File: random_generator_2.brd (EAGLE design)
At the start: 19.1 x 19.1 mm, 17 parts, among them IC1 OPA2340U

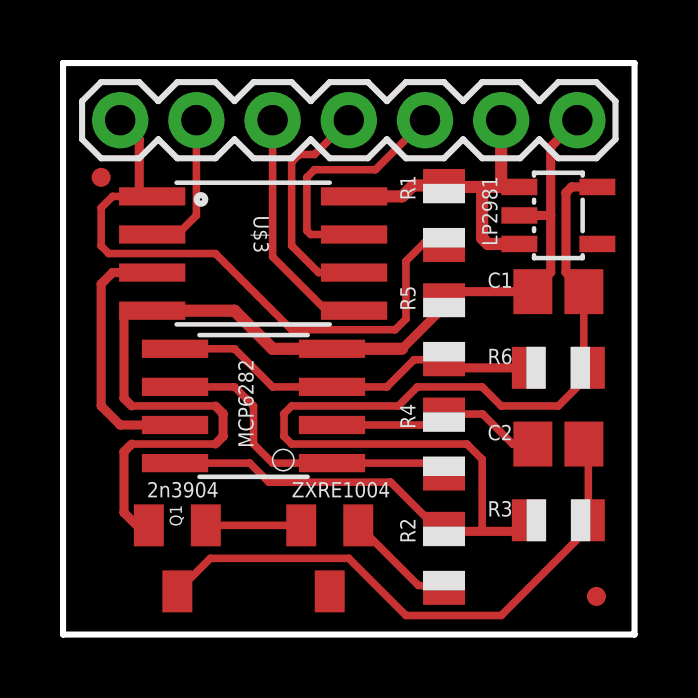
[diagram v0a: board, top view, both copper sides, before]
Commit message: MANY BUGS! NOW, HANDLE IT!
A whole nightmarish mess of bugs fixed: Dr Nyquist prescribed some
faster sampling, (just in case). I also tied op amp to VCCIO instead of
3V (for voltage swings guaranteed to trigger logic high), SPI/USI code
now works too. WIll upload an Arduino test program soon…
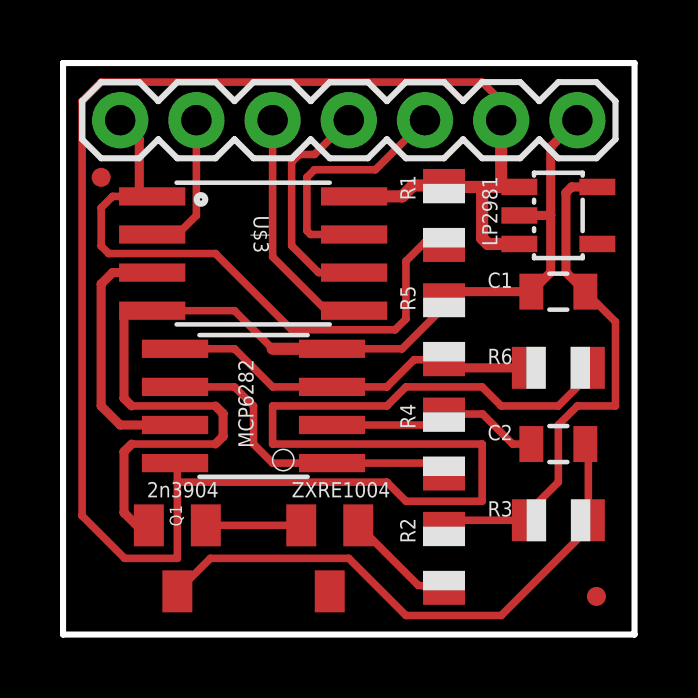
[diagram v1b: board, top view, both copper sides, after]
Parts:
- C1: device adafruit:C0805 -> SparkFun:0805
- C2: value .1uF -> 1uF; device adafruit:C0805 -> SparkFun:0805
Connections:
- net V+: no longer IC1.8, R6.2
- net VCCIO: now also IC1.8, R6.2
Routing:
- net VCCIO: track 11.5 -> 79.8 mm
- net V+: track 43.6 -> 17.6 mm
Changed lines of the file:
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@@
 <setting verticaltext="up"/>
 </settings>
-<grid distance="0.05" unitdist="inch" unit="inch" style="lines" multiple="1" display="yes" altdistance="0.01" altunitdist="inch" altunit="inch"/>
+<grid distance="0.05" unitdist="inch" unit="inch" style="lines" multiple="1" display="yes" altdistance="0.025" altunitdist="inch" altunit="inch"/>
 <layers>
 <layer number="1" name="Top" color="4" fill="1" visible="yes" active="yes"/>
@@
 <attribute name="VALUE" x="14.986" y="8.89" size="0.508" layer="27" font="vector" rot="R180"/>
 </element>
-<element name="C2" library="adafruit" package="C0805" value=".1uF" x="16.51" y="6.35" smashed="yes" rot="R180">
+<element name="C2" library="SparkFun" package="0805" value="1uF" x="16.51" y="6.35" smashed="yes" rot="R180">
 <attribute name="NAME" x="14.986" y="6.985" size="0.508" layer="25" font="vector" rot="R180"/>
 <attribute name="VALUE" x="14.986" y="6.35" size="0.508" layer="27" font="vector" rot="R180"/>
 </element>
 <element name="U$2" library="hjohnson_library" package="SOT23-5L" value="TC1014" x="16.51" y="13.97" smashed="yes" rot="R270"/>
-<element name="C1" library="adafruit" package="C0805" value="1uF" x="16.51" y="11.43" smashed="yes" rot="R180">
+<element name="C1" library="SparkFun" package="0805" value="1uF" x="16.51" y="11.43" smashed="yes" rot="R180">
 <attribute name="NAME" x="14.986" y="12.065" size="0.508" layer="25" font="vector" rot="R180"/>
 <attribute name="VALUE" x="14.986" y="11.43" size="0.508" layer="27" font="vector" rot="R180"/>
@@
 <wire x1="5.08" y1="7.62" x2="2.286" y2="7.62" width="0.254" layer="1"/>
 <wire x1="8.9662" y1="9.525" x2="6.985" y2="9.525" width="0.4064" layer="1"/>
-<wire x1="6.985" y1="9.525" x2="5.715" y2="10.795" width="0.4064" layer="1"/>
-<wire x1="5.715" y1="10.795" x2="2.9718" y2="10.795" width="0.4064" layer="1"/>
-<wire x1="8.9662" y1="9.525" x2="11.303" y2="9.525" width="0.4064" layer="1"/>
+<wire x1="6.985" y1="9.525" x2="5.715" y2="10.795" width="0.254" layer="1"/>
+<wire x1="5.715" y1="10.795" x2="2.9718" y2="10.795" width="0.254" layer="1"/>
+<wire x1="8.9662" y1="9.525" x2="11.303" y2="9.525" width="0.254" layer="1"/>
 <wire x1="12.7" y1="11.16" x2="12.7" y2="10.922" width="0.254" layer="1"/>
-<wire x1="12.7" y1="10.922" x2="11.303" y2="9.525" width="0.3048" layer="1"/>
+<wire x1="12.7" y1="10.922" x2="11.303" y2="9.525" width="0.254" layer="1"/>
 <contactref element="JP1" pad="7"/>
-<wire x1="16.256" y1="12.076" x2="15.66" y2="11.43" width="0.3048" layer="1"/>
+<wire x1="16.256" y1="12.076" x2="15.61" y2="11.43" width="0.3048" layer="1"/>
 <wire x1="17.145" y1="17.145" x2="16.256" y2="16.256" width="0.3048" layer="1"/>
 <wire x1="16.256" y1="16.256" x2="16.256" y2="13.97" width="0.3048" layer="1"/>
 <wire x1="16.256" y1="13.97" x2="16.256" y2="12.076" width="0.3048" layer="1"/>
 <wire x1="15.21" y1="13.97" x2="16.256" y2="13.97" width="0.3048" layer="1"/>
-<wire x1="15.66" y1="11.43" x2="12.97" y2="11.43" width="0.3048" layer="1"/>
+<wire x1="15.61" y1="11.43" x2="12.97" y2="11.43" width="0.3048" layer="1"/>
 <wire x1="12.97" y1="11.43" x2="12.7" y2="11.16" width="0.3048" layer="1"/>
 </signal>
@@
 <contactref element="R2" pad="2"/>
 <contactref element="R3" pad="2"/>
-<contactref element="R6" pad="2"/>
 <contactref element="U$2" pad="5"/>
 <contactref element="C1" pad="1"/>
-<contactref element="IC1" pad="8"/>
-<contactref element="IC1" pad="8"/>
-<wire x1="15.51" y1="3.81" x2="15.748" y2="3.81" width="0.254" layer="1"/>
-<wire x1="6.858" y1="5.08" x2="10.922" y2="5.08" width="0.254" layer="1"/>
-<wire x1="10.922" y1="5.08" x2="12.7" y2="3.302" width="0.254" layer="1"/>
-<wire x1="12.7" y1="3.54" x2="12.7" y2="3.302" width="0.254" layer="1"/>
-<wire x1="15.378" y1="3.44" x2="15.748" y2="3.81" width="0.2032" layer="1"/>
 <wire x1="17.81" y1="14.92" x2="16.952" y2="14.92" width="0.3048" layer="1"/>
 <wire x1="16.764" y1="14.732" x2="16.764" y2="12.076" width="0.3048" layer="1"/>
-<wire x1="16.764" y1="12.076" x2="17.36" y2="11.43" width="0.3048" layer="1"/>
+<wire x1="16.764" y1="12.076" x2="17.41" y2="11.43" width="0.3048" layer="1"/>
 <wire x1="16.952" y1="14.92" x2="16.764" y2="14.732" width="0.3048" layer="1"/>
-<wire x1="15.378" y1="3.44" x2="12.8" y2="3.44" width="0.3048" layer="1"/>
-<wire x1="12.8" y1="3.44" x2="12.7" y2="3.54" width="0.254" layer="1"/>
-<wire x1="17.51" y1="8.89" x2="17.36" y2="8.89" width="0.254" layer="1"/>
-<wire x1="17.36" y1="8.89" x2="17.36" y2="11.43" width="0.254" layer="1"/>
-<wire x1="17.36" y1="8.89" x2="17.36" y2="8.47" width="0.254" layer="1"/>
-<wire x1="17.36" y1="8.47" x2="16.51" y2="7.62" width="0.254" layer="1"/>
-<wire x1="16.51" y1="7.62" x2="14.605" y2="7.62" width="0.254" layer="1"/>
-<wire x1="14.605" y1="7.62" x2="13.97" y2="8.255" width="0.254" layer="1"/>
-<wire x1="13.462" y1="6.35" x2="13.97" y2="5.842" width="0.254" layer="1"/>
-<wire x1="13.97" y1="5.842" x2="13.97" y2="3.556" width="0.254" layer="1"/>
-<wire x1="12.8" y1="3.44" x2="13.854" y2="3.44" width="0.254" layer="1"/>
-<wire x1="13.854" y1="3.44" x2="13.97" y2="3.556" width="0.254" layer="1"/>
-<wire x1="13.97" y1="8.255" x2="11.811" y2="8.255" width="0.254" layer="1"/>
-<wire x1="11.811" y1="8.255" x2="11.176" y2="7.62" width="0.254" layer="1"/>
-<wire x1="13.462" y1="6.35" x2="7.62" y2="6.35" width="0.254" layer="1"/>
-<wire x1="7.62" y1="6.35" x2="7.366" y2="6.604" width="0.254" layer="1"/>
-<wire x1="7.366" y1="6.604" x2="7.366" y2="7.366" width="0.254" layer="1"/>
-<wire x1="7.62" y1="7.62" x2="11.176" y2="7.62" width="0.254" layer="1"/>
-<wire x1="3.7338" y1="5.715" x2="6.223" y2="5.715" width="0.254" layer="1"/>
-<wire x1="6.223" y1="5.715" x2="6.858" y2="5.08" width="0.254" layer="1"/>
-<wire x1="7.366" y1="7.366" x2="7.62" y2="7.62" width="0.254" layer="1"/>
+<wire x1="15.51" y1="3.81" x2="12.97" y2="3.81" width="0.254" layer="1"/>
+<wire x1="12.97" y1="3.81" x2="12.7" y2="3.54" width="0.254" layer="1"/>
+<wire x1="15.51" y1="3.81" x2="15.51" y2="4.08" width="0.254" layer="1"/>
+<wire x1="15.51" y1="4.08" x2="16.51" y2="5.08" width="0.254" layer="1"/>
+<wire x1="16.51" y1="5.08" x2="16.51" y2="6.985" width="0.254" layer="1"/>
+<wire x1="16.51" y1="6.985" x2="17.145" y2="7.62" width="0.254" layer="1"/>
+<wire x1="17.145" y1="7.62" x2="18.415" y2="7.62" width="0.254" layer="1"/>
+<wire x1="18.415" y1="7.62" x2="18.415" y2="10.425" width="0.254" layer="1"/>
+<wire x1="18.415" y1="10.425" x2="17.41" y2="11.43" width="0.254" layer="1"/>
 </signal>
 <signal name="N$2">
@@
 <wire x1="11.43" y1="0.635" x2="14.605" y2="0.635" width="0.254" layer="1"/>
 <wire x1="14.605" y1="0.635" x2="17.41" y2="3.44" width="0.254" layer="1"/>
-<wire x1="17.36" y1="6.35" x2="17.51" y2="6.35" width="0.254" layer="1"/>
+<wire x1="17.41" y1="6.35" x2="17.51" y2="6.35" width="0.254" layer="1"/>
 <wire x1="17.51" y1="6.35" x2="17.51" y2="3.81" width="0.254" layer="1"/>
 </signal>
@@
 <wire x1="12.7" y1="7.35" x2="13.986" y2="7.35" width="0.254" layer="1"/>
 <wire x1="13.986" y1="7.35" x2="14.986" y2="6.35" width="0.254" layer="1"/>
-<wire x1="14.986" y1="6.35" x2="15.66" y2="6.35" width="0.254" layer="1"/>
+<wire x1="14.986" y1="6.35" x2="15.61" y2="6.35" width="0.254" layer="1"/>
 </signal>
 <signal name="N$6">
@@
 <wire x1="11.668" y1="14.97" x2="11.303" y2="14.605" width="0.4064" layer="1"/>
 <wire x1="9.7028" y1="14.605" x2="11.303" y2="14.605" width="0.4064" layer="1"/>
+<contactref element="R6" pad="2"/>
+<contactref element="IC1" pad="8"/>
+<wire x1="3.7338" y1="5.715" x2="3.81" y2="5.715" width="0.254" layer="1"/>
+<wire x1="3.81" y1="5.715" x2="3.81" y2="5.08" width="0.254" layer="1"/>
+<wire x1="3.81" y1="5.08" x2="3.81" y2="2.54" width="0.254" layer="1"/>
+<wire x1="3.81" y1="2.54" x2="2.054903125" y2="2.54" width="0.254" layer="1"/>
+<wire x1="2.054903125" y1="2.54" x2="0.635" y2="3.959903125" width="0.254" layer="1"/>
+<wire x1="0.635" y1="3.959903125" x2="0.635" y2="17.78" width="0.254" layer="1"/>
+<wire x1="0.635" y1="17.78" x2="1.27" y2="18.415" width="0.254" layer="1"/>
+<wire x1="1.27" y1="18.415" x2="13.97" y2="18.415" width="0.254" layer="1"/>
+<wire x1="13.97" y1="18.415" x2="14.605" y2="17.78" width="0.254" layer="1"/>
+<wire x1="14.605" y1="17.78" x2="14.605" y2="17.145" width="0.254" layer="1"/>
+<wire x1="17.51" y1="8.89" x2="17.51" y2="8.62" width="0.254" layer="1"/>
+<wire x1="17.51" y1="8.62" x2="16.51" y2="7.62" width="0.254" layer="1"/>
+<wire x1="16.51" y1="7.62" x2="14.605" y2="7.62" width="0.254" layer="1"/>
+<wire x1="14.605" y1="7.62" x2="13.97" y2="8.255" width="0.254" layer="1"/>
+<wire x1="13.97" y1="8.255" x2="11.43" y2="8.255" width="0.254" layer="1"/>
+<wire x1="11.43" y1="8.255" x2="10.795" y2="7.62" width="0.254" layer="1"/>
+<wire x1="10.795" y1="7.62" x2="6.985" y2="7.62" width="0.254" layer="1"/>
+<wire x1="6.985" y1="7.62" x2="6.985" y2="6.35" width="0.254" layer="1"/>
+<wire x1="6.985" y1="6.35" x2="13.97" y2="6.35" width="0.254" layer="1"/>
+<wire x1="13.97" y1="6.35" x2="13.97" y2="4.445" width="0.254" layer="1"/>
+<wire x1="13.97" y1="4.445" x2="11.43" y2="4.445" width="0.254" layer="1"/>
+<wire x1="11.43" y1="4.445" x2="10.795" y2="5.08" width="0.254" layer="1"/>
+<wire x1="10.795" y1="5.08" x2="3.81" y2="5.08" width="0.254" layer="1"/>
 </signal>
 <signal name="MISO">

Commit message: Updates to BOM/Quote, and slight update to board: tweaked everything around a bit to give easier PnP placement
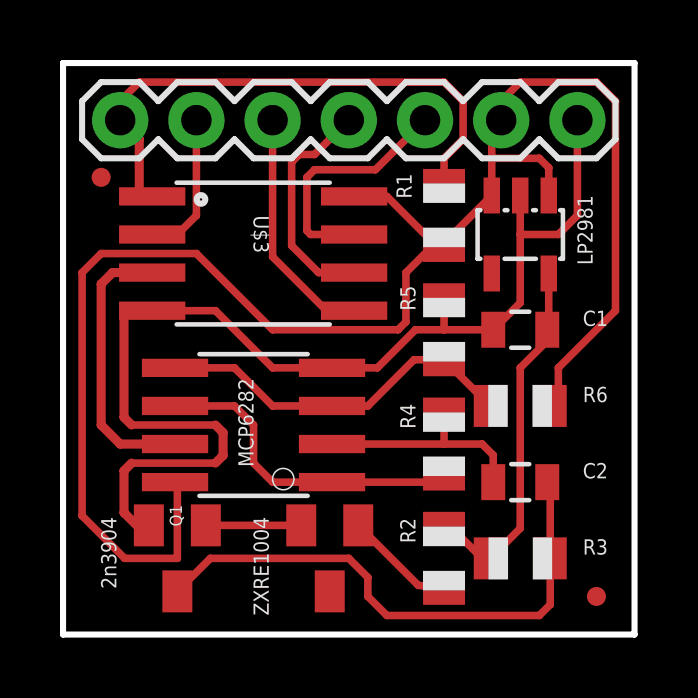
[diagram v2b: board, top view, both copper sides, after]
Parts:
- moved R6 1.80 mm to (15.2, 7.62)
- moved R3 1.80 mm to (15.2, 2.54)
- moved C1 1.80 mm to (15.2, 10.2)
- moved C2 1.80 mm to (15.2, 5.08)
- moved U$2 1.42 mm to (15.2, 13.3), turned to 180 degrees
- moved IC1 0.63 mm to (6.35, 6.99)
- moved U$4 0.63 mm to (2.54, 5.71)
- turned R1 to 270 degrees
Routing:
- net VCCIO: track 79.8 -> 58.2 mm
- net V+: track 17.6 -> 12.3 mm
- net /RES: track 21.7 -> 19.1 mm
- net GND: track 36.1 -> 38.5 mm
- net N$3: track 19.0 -> 18.3 mm
- net RANDOM: track 8.65 -> 9.29 mm

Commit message: Added/fixed comments in firmware, made component designators a bit bigger.
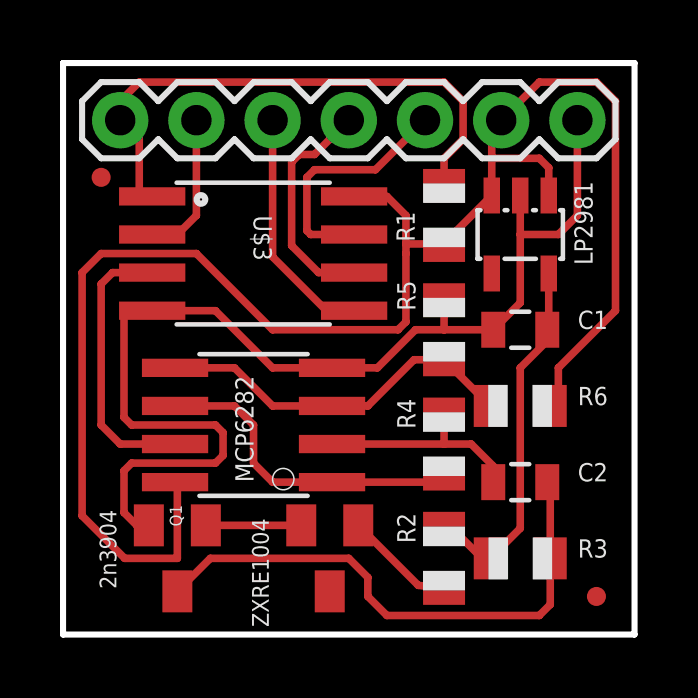
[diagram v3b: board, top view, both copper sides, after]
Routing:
- net VCCIO: track 58.2 -> 57.3 mm
